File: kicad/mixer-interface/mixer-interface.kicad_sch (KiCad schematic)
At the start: 25 parts, among them J1 PWR_IN, J2 CAN, J3 FAN, Q2 NCEP60T20, U1 AMS1117-5.0, U10 ESP32-DEVKITC-32U, U2 TIME_ENCODER, U3 SPEED_ENCODER, U4 DS18B20, U5 DS18B20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

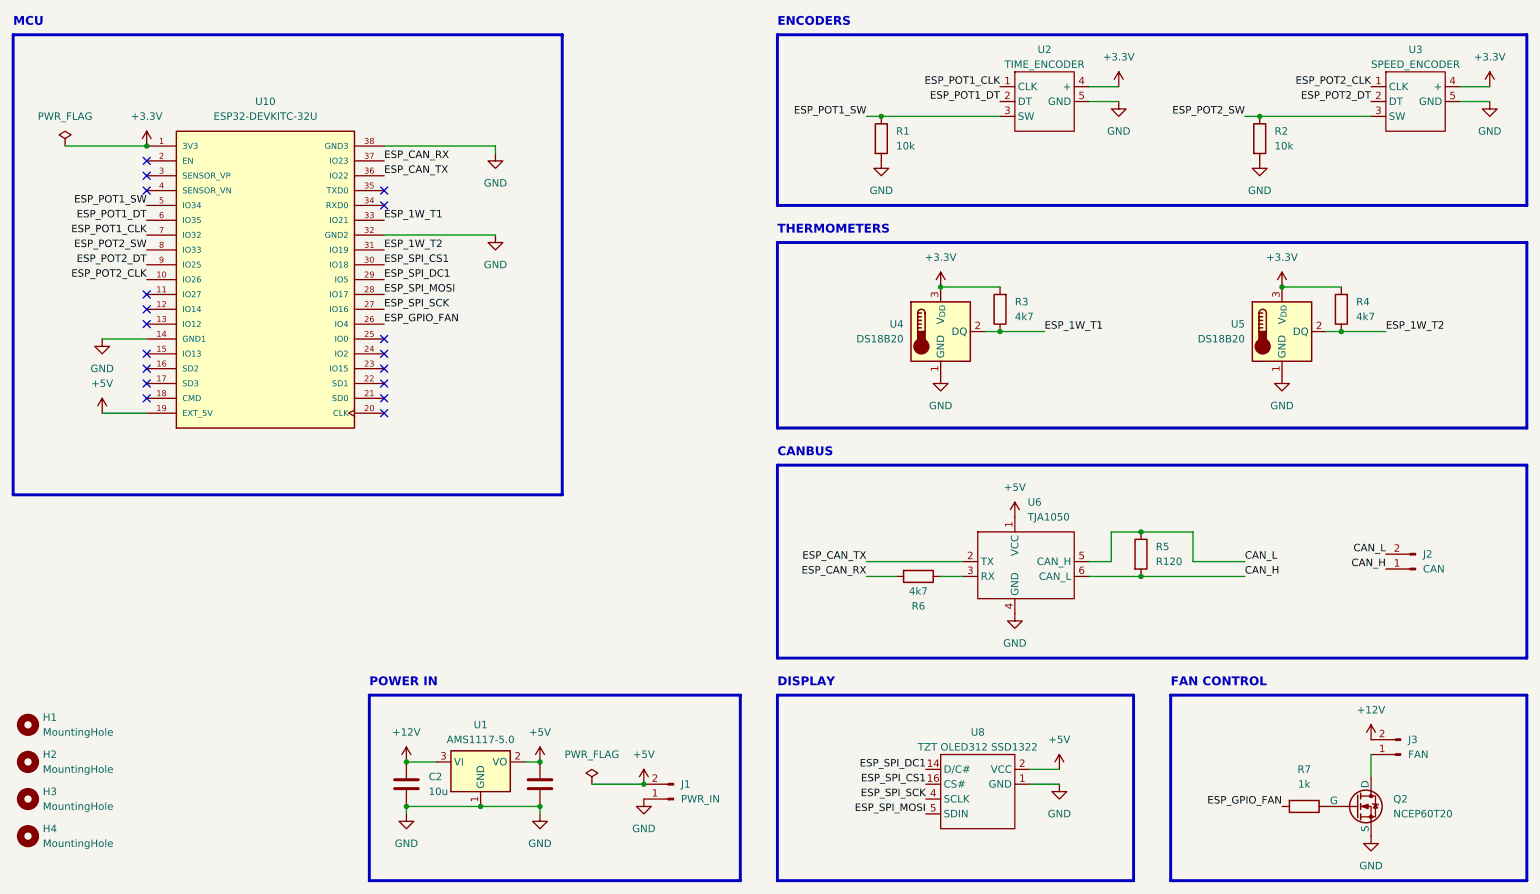
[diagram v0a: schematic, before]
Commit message: Added encoder breakout and updated other projects
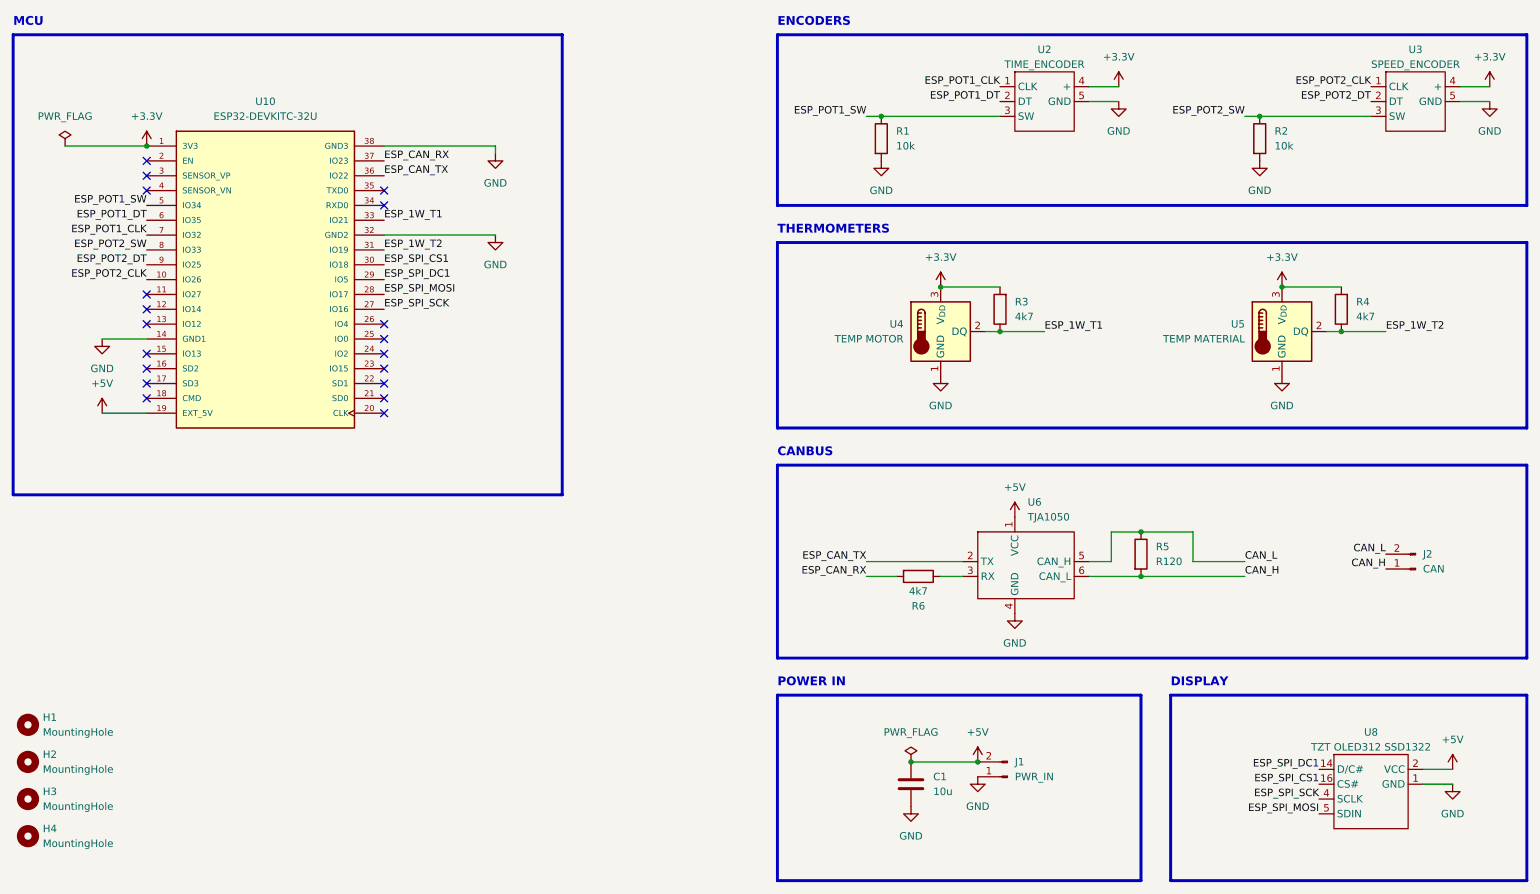
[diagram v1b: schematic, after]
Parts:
- removed C2, C4: 10u, Capacitor_SMD:C_0805_2012Metric, symbol Device:C
- removed J3: FAN, Connector_JST:JST_XH_B2B-XH-AM_1x02_P2.50mm_Vertical, symbol Connector:Conn_01x02_Pin
- removed Q2: NCEP60T20, --local:TO-220-3_Horizontal_TabUp_no_hole, symbol Simulation_SPICE:NMOS
- removed R7: 1k, Resistor_SMD:R_0805_2012Metric_Pad1.20x1.40mm_HandSolder, symbol Device:R
- removed U1: AMS1117-5.0, Package_TO_SOT_SMD:SOT-223-3_TabPin2, symbol Regulator_Linear:AMS1117-5.0
- added C1: 10u, Capacitor_SMD:C_0805_2012Metric, symbol Device:C
- H1, H2, H3, H4: footprint MountingHole:MountingHole_3.2mm_M3 -> MountingHole:MountingHole_3.2mm_M3_Pad_Via
- U4: value DS18B20 -> TEMP MOTOR
- U5: value DS18B20 -> TEMP MATERIAL
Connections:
- net +5V: now also C1.1
- net GND: now also C1.2
- net ESP_GPIO_FAN: no longer names the net of U10.26 (IO4)
- no-connect marks 18 -> 19
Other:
- note removed: "FAN CONTROL"
- moved on the sheet: J1, U8

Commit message: Final updates for manufacturing
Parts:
- J1, J2: footprint Connector_JST:JST_XH_B2B-XH-AM_1x02_P2.50mm_Vertical -> Connector_JST:JST_XH_B2B-XH-A_1x02_P2.50mm_Vertical
- U2, U3: footprint Connector_JST:JST_XH_B5B-XH-AM_1x05_P2.50mm_Vertical -> Connector_JST:JST_XH_B5B-XH-A_1x05_P2.50mm_Vertical
- U4, U5: footprint Connector_JST:JST_XH_B3B-XH-AM_1x03_P2.50mm_Vertical -> Connector_JST:JST_XH_B3B-XH-A_1x03_P2.50mm_Vertical
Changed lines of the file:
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@@
       (effects (font (size 1.27 1.27)) (justify right))
     )
-    (property "Footprint" "Connector_JST:JST_XH_B2B-XH-AM_1x02_P2.50mm_Vertical" (at 260.35 109.22 0)
+    (property "Footprint" "Connector_JST:JST_XH_B2B-XH-A_1x02_P2.50mm_Vertical" (at 260.35 109.22 0)
       (effects (font (size 1.27 1.27)) hide)
     )
@@
       (effects (font (size 1.27 1.27)) (justify right))
     )
-    (property "Footprint" "Connector_JST:JST_XH_B2B-XH-AM_1x02_P2.50mm_Vertical" (at 190.5 144.78 0)
+    (property "Footprint" "Connector_JST:JST_XH_B2B-XH-A_1x02_P2.50mm_Vertical" (at 190.5 144.78 0)
       (effects (font (size 1.27 1.27)) hide)
     )
@@
       (effects (font (size 1.27 1.27)) (justify right))
     )
-    (property "Footprint" "Connector_JST:JST_XH_B3B-XH-AM_1x03_P2.50mm_Vertical" (at 212.09 74.93 0)
+    (property "Footprint" "Connector_JST:JST_XH_B3B-XH-A_1x03_P2.50mm_Vertical" (at 212.09 74.93 0)
       (effects (font (size 1.27 1.27)) hide)
     )
@@
       (effects (font (size 1.27 1.27)))
     )
-    (property "Footprint" "Connector_JST:JST_XH_B5B-XH-AM_1x05_P2.50mm_Vertical" (at 189.23 22.86 0)
+    (property "Footprint" "Connector_JST:JST_XH_B5B-XH-A_1x05_P2.50mm_Vertical" (at 189.23 22.86 0)
       (effects (font (size 1.27 1.27)) hide)
     )
@@
       (effects (font (size 1.27 1.27)) (justify right))
     )
-    (property "Footprint" "Connector_JST:JST_XH_B3B-XH-AM_1x03_P2.50mm_Vertical" (at 153.67 74.93 0)
+    (property "Footprint" "Connector_JST:JST_XH_B3B-XH-A_1x03_P2.50mm_Vertical" (at 153.67 74.93 0)
       (effects (font (size 1.27 1.27)) hide)
     )
@@
       (effects (font (size 1.27 1.27)))
     )
-    (property "Footprint" "Connector_JST:JST_XH_B5B-XH-AM_1x05_P2.50mm_Vertical" (at 252.73 22.86 0)
-      (effects (font (size 1.27 1.27)) hide)
-    )
+    (property "Footprint" "Connector_JST:JST_XH_B5B-XH-A_1x05_P2.50mm_Vertical" (at 252.73 22.86 0)
+      (effects (font (size 1.27 1.27)) hide)
+    )
